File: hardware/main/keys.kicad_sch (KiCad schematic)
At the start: 134 parts, among them SW1 Esc, SW10 a, SW12 Fn, SW13 F2, SW14 2, SW15 w, SW16 s, SW17 z, SW18 Tux, SW19 F3, SW2 F1, SW20 3, SW21 e, SW22 d, SW23 c, SW24 Alt, SW25 F4, SW26 4, SW27 r, SW28 f, SW29 v, SW3 tilde, SW31 F5, SW32 5, SW33 t, SW34 g, SW35 b, SW36 F6, SW37 6, SW38 y, SW39 h, SW4 Tab, SW40 n, SW41 F7, SW42 7, SW43 u, SW44 j, SW45 m, SW46 Space, SW47 F8, SW48 8, SW49 i, SW5 Caps Lock, SW50 k, SW51 ,, SW52 F9, SW53 9, SW54 o, SW55 l, SW56 ., SW57 F10, SW58 0, SW59 p, SW6 Shift, SW60 ;, SW61 /, SW62 Alt Gr, SW63 F11, SW64 -, SW65 [, SW66 ', SW67 Menu, SW68 F12, SW69 =, SW7 Ctrl, SW70 ], SW71 \, SW72 Shift, SW73 Ctrl, SW74 Print, SW75 Backspace, SW76 Enter, SW77 Left, SW78 Scroll Lock, SW79 Up, SW8 1, SW80 Down, SW81 Pause, SW82 INS, SW83 DEL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

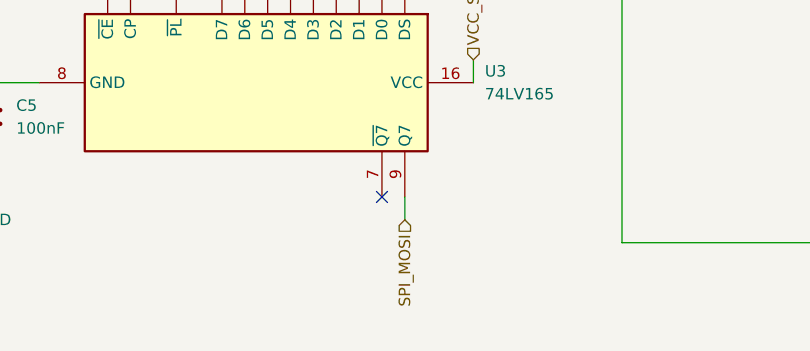
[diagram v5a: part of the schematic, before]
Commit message: Fix MISO label for the shift registers
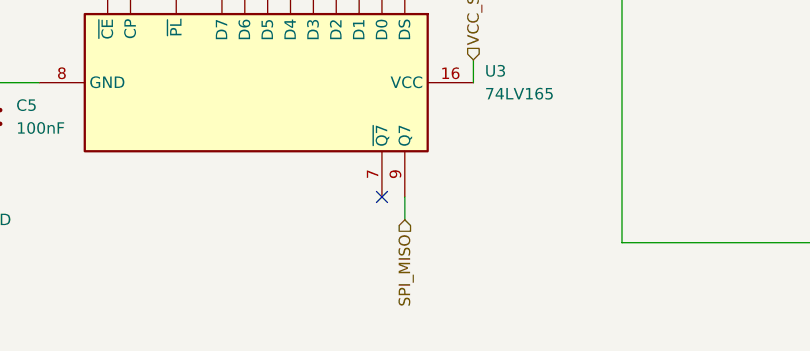
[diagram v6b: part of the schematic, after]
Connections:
- net SPI_MOSI: no longer U3.9 (Q7)
- new net SPI_MISO: U3.9 (Q7)
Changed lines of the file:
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@@
     (effects (font (size 1.27 1.27)) (justify left))
   )
-  (hierarchical_label "SPI_MOSI" (shape input) (at 127 236.22 270)
+  (hierarchical_label "SPI_MISO" (shape input) (at 127 236.22 270)
     (effects (font (size 1.27 1.27)) (justify right))
   )

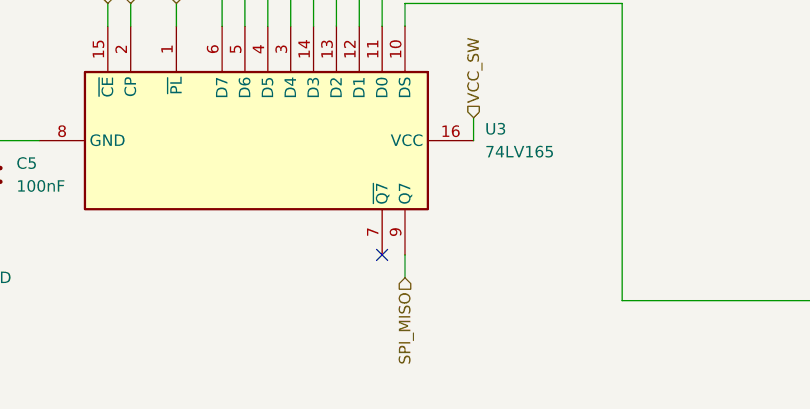
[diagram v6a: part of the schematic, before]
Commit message: Add connections to the NRF module
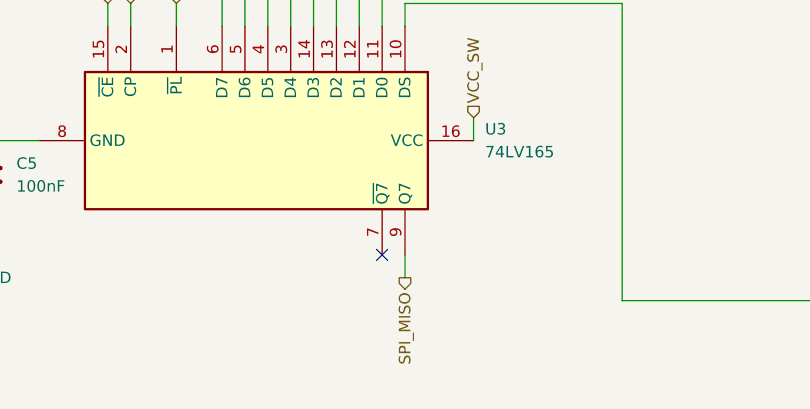
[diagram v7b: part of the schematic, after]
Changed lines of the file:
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@@
     (effects (font (size 1.27 1.27)) (justify left))
   )
-  (hierarchical_label "SPI_MISO" (shape input) (at 127 236.22 270)
+  (hierarchical_label "SPI_MISO" (shape output) (at 127 236.22 270)
     (effects (font (size 1.27 1.27)) (justify right))
   )

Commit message: Add footprints to many symbols
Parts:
- C4, C5, C6: footprint (none) -> Capacitor_SMD:C_0201_0603Metric_Pad0.64x0.40mm_HandSolder; Mouser (none) -> 581-06033C104KAT4A; Part Name (none) -> 06033C104KAT4A
- SW1, SW10, SW12, SW13, SW14, SW15, SW16, SW17, SW18, SW19, SW2, SW20, SW21, SW22, SW23, SW24, SW25, SW26, SW27, SW28, SW29, SW3, SW31, SW32, SW33, SW34, SW35, SW36, SW37, SW38, SW39, SW4, SW40, SW41, SW42, SW43, SW44, SW45, SW46, SW47, SW48, SW49, SW5, SW50, SW51, SW52, SW53, SW54, SW55, SW56, SW57, SW58, SW59, SW6, SW60, SW61, SW62, SW63, SW64, SW65, SW66, SW67, SW68, SW69, SW7, SW70, SW71, SW72, SW73, SW74, SW75, SW76, SW77, SW78, SW79, SW8, SW80, SW81, SW82, SW83, SW84, SW85, SW86, SW87, SW9: Mouser (none) -> 540-MX1A-E1NW; Part Name (none) -> MX1A-E1NW
